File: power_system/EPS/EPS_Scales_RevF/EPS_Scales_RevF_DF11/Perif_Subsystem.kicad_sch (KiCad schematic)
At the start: 40 parts, among them CN1 DF11-16DP-2DSA(08), U12 TPS1HB08BQPWPRQ1, U13 LT8612EUDE#PBF, U16 INA260AIPWR

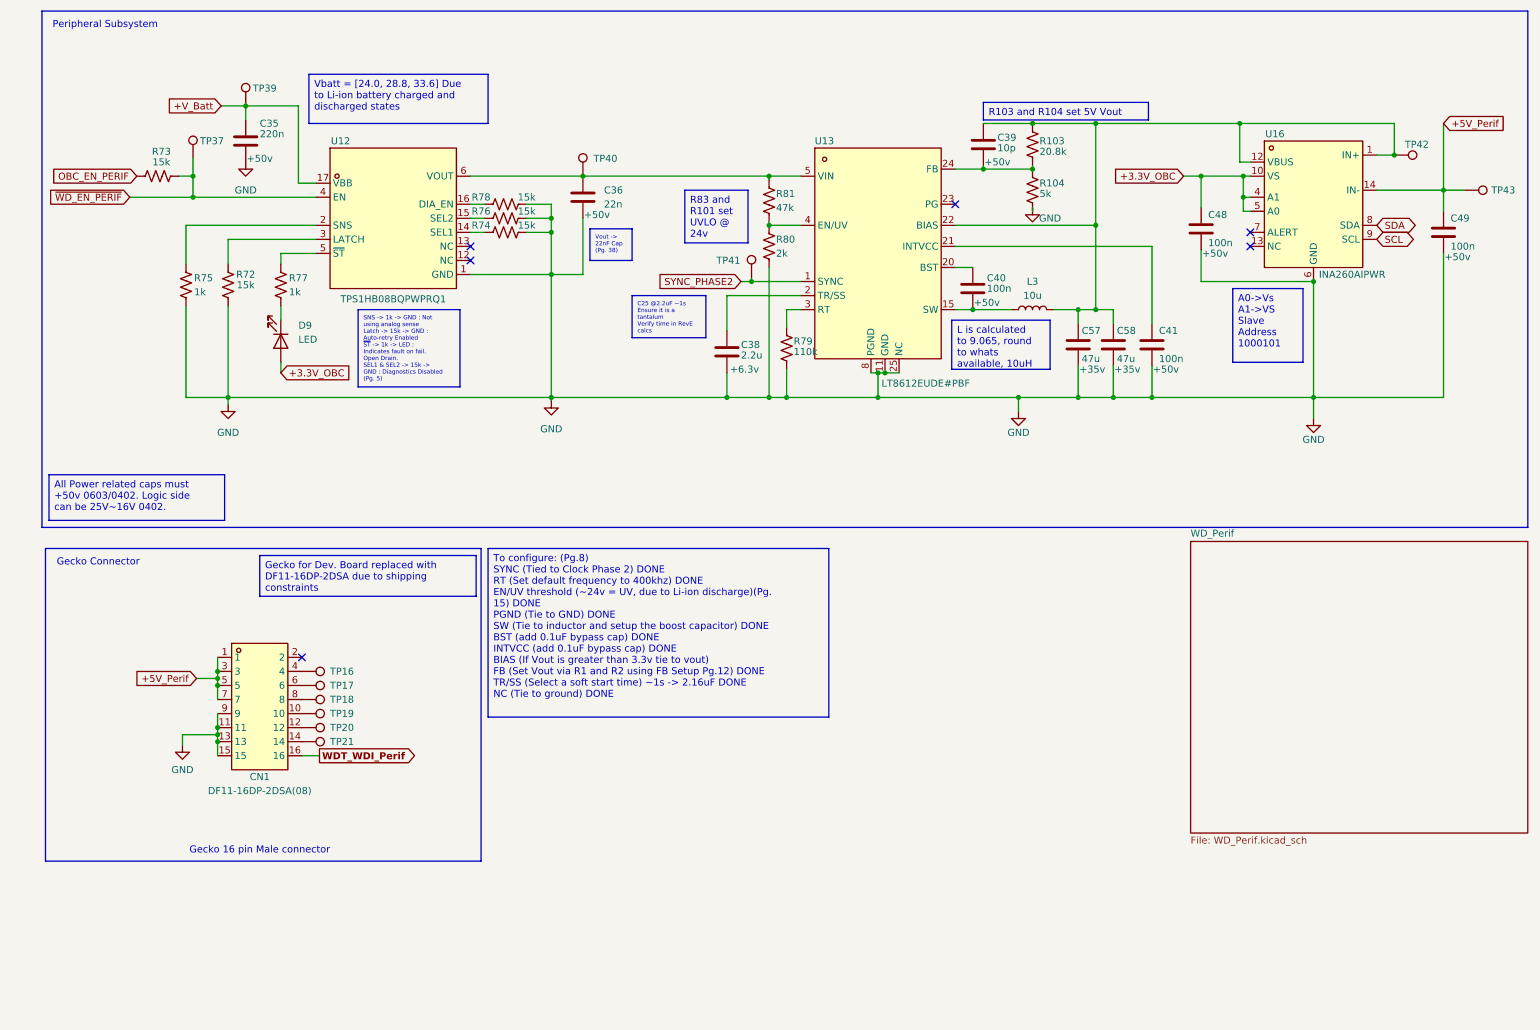
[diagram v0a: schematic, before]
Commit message: Completed EPS REV F / Viking 1-C PCB
Fixed minor issue with the extra resistor for the EN line VD, and added temperature sensors for each subsystem.
Also, the JPL logo is back!
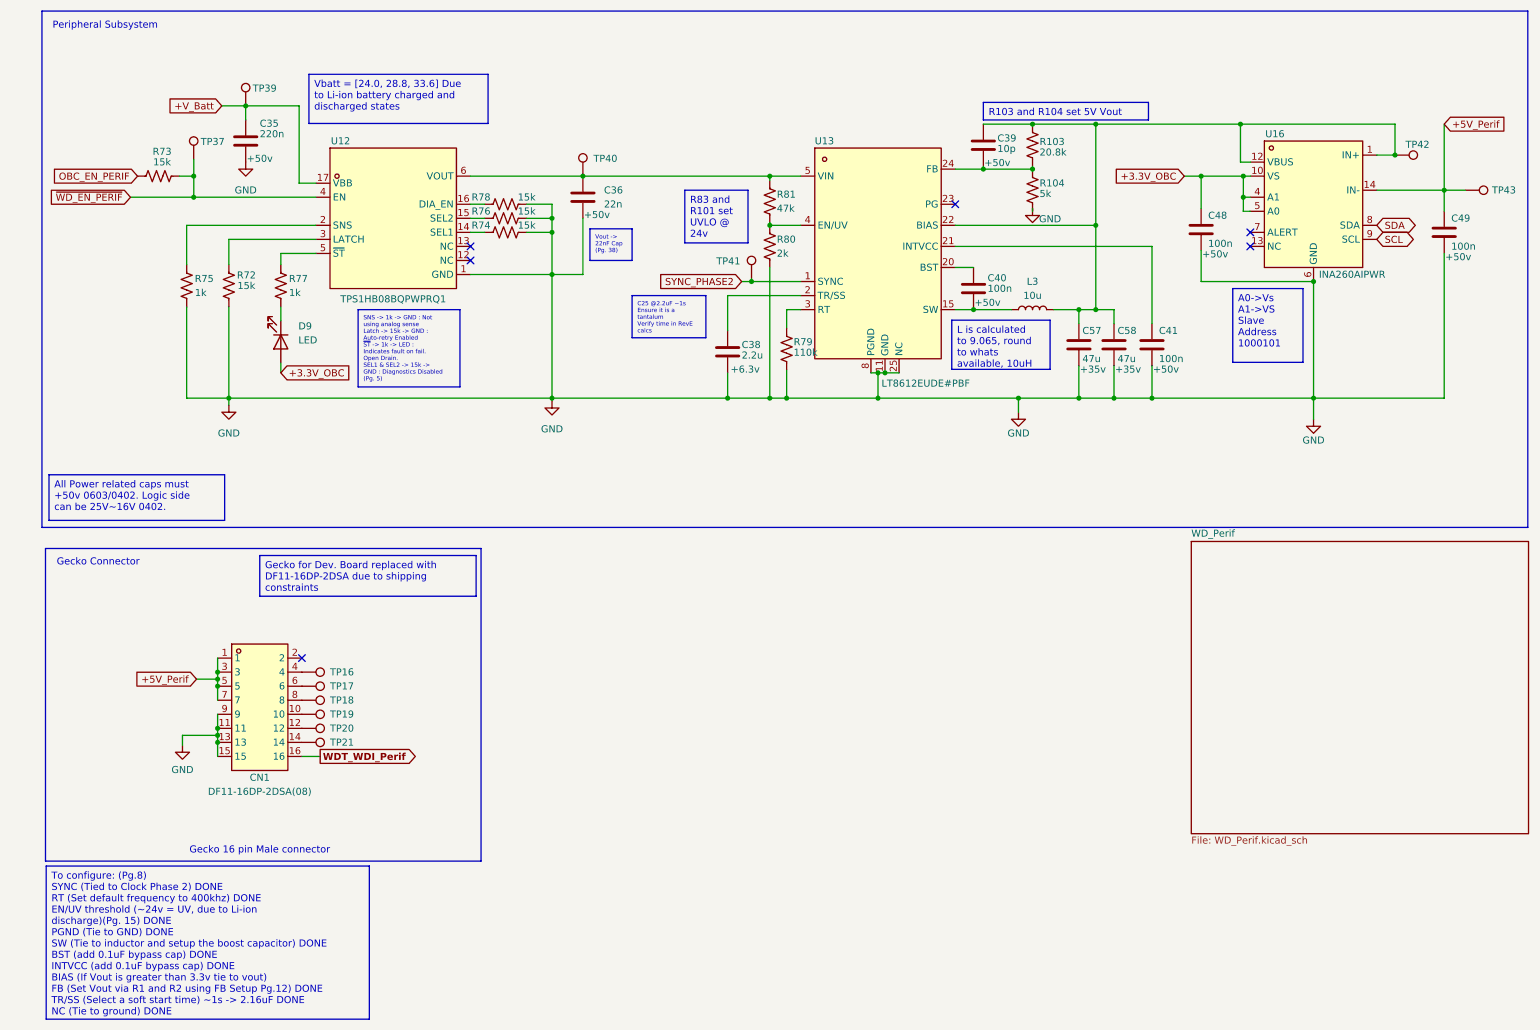
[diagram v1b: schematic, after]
